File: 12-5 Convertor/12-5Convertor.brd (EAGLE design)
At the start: 29.6 x 41.3 mm, 14 parts, among them U1 LM2678

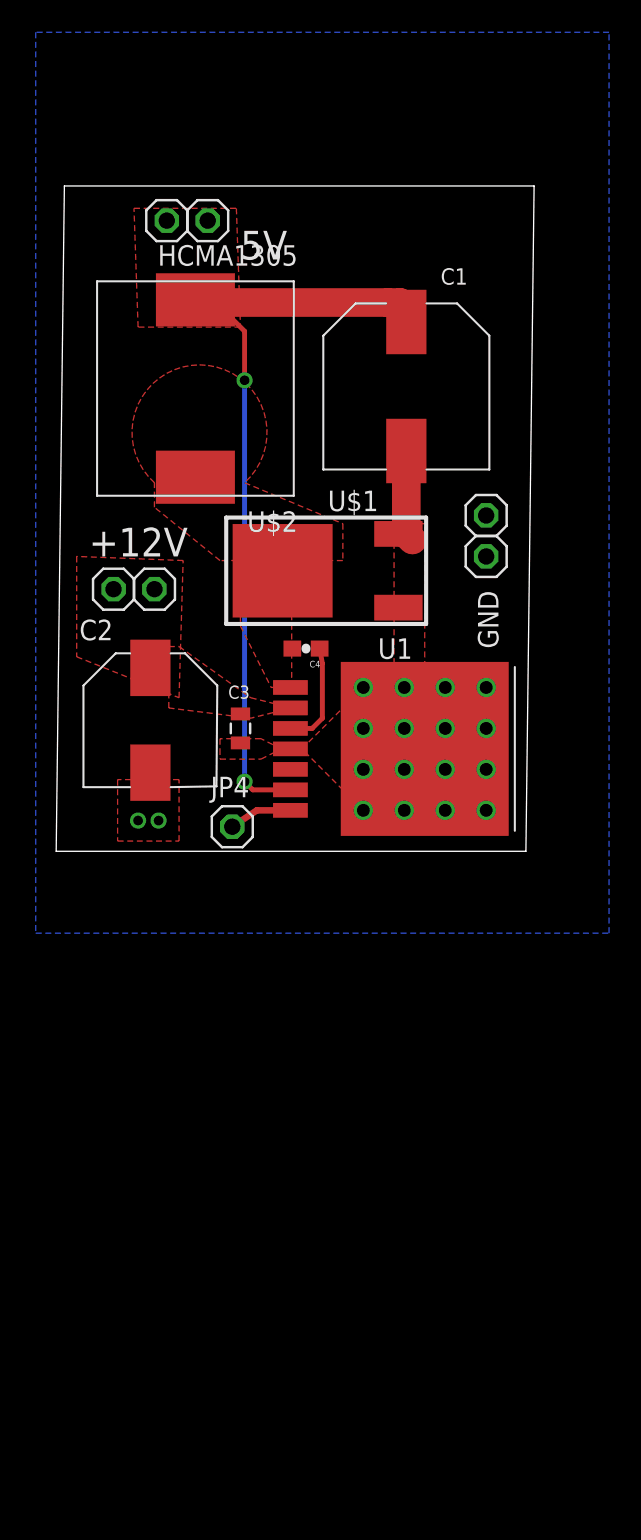
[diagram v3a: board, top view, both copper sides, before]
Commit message: Put finishing touches on buck regulator test board
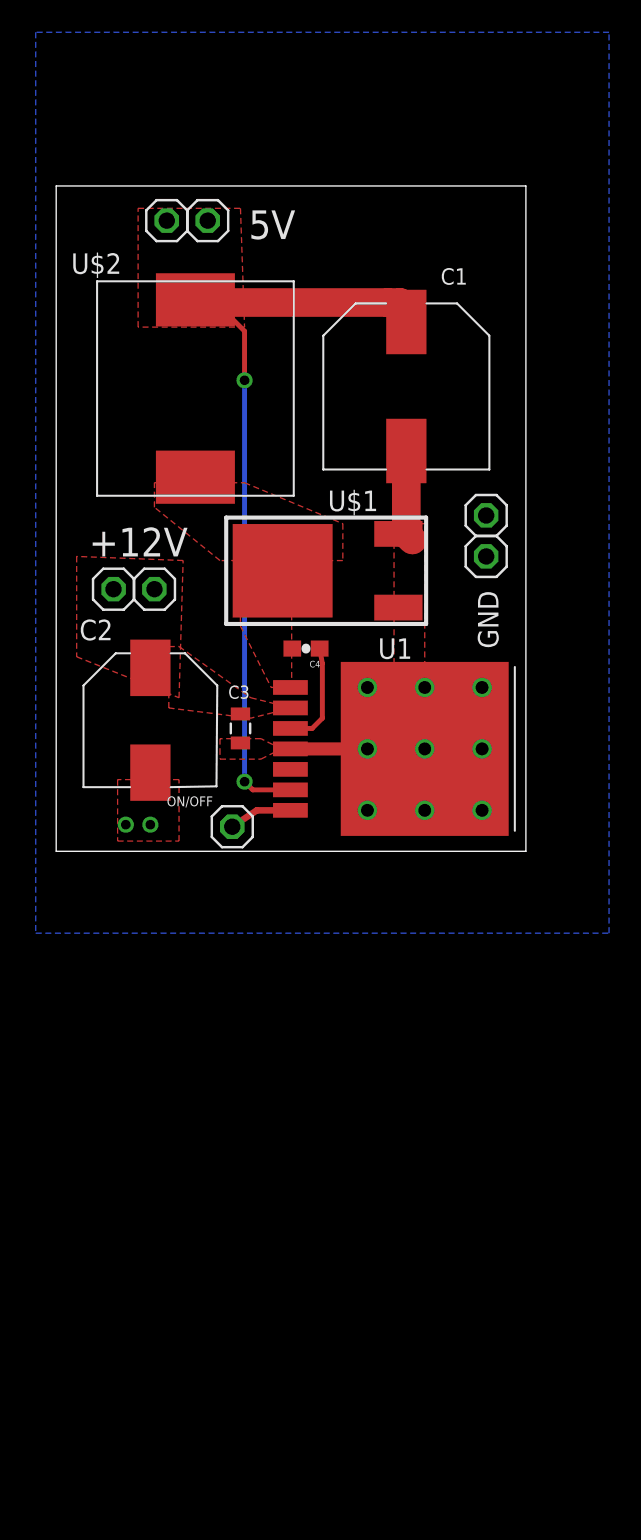
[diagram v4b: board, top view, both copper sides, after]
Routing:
- net GND: track 5.68 -> 10.5 mm, vias 18 -> 11
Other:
- board size 29.6 x 41.3 mm -> 29.1 x 41.3 mm
- board text added: "Designed by Luke McBee, Richard Shen, Jeff Geiss, and Dimcho Karakashev +12V to +5V Buck Regulator 11/8/2015"
- board text added: "ON/OFF"
- board text removed: "DC-DC 12V-5V Convertor"
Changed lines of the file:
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@@
 <plain>
 <wire x1="31.75" y1="17.78" x2="60.884" y2="17.78" width="0" layer="20"/>
-<wire x1="60.884" y1="17.78" x2="61.392" y2="59.045" width="0" layer="20"/>
-<wire x1="61.392" y1="59.045" x2="32.258" y2="59.045" width="0" layer="20"/>
-<wire x1="32.258" y1="59.045" x2="31.75" y2="17.78" width="0" layer="20"/>
+<wire x1="60.884" y1="17.78" x2="60.884" y2="59.045" width="0" layer="20"/>
+<wire x1="60.884" y1="59.045" x2="31.75" y2="59.045" width="0" layer="20"/>
+<wire x1="31.75" y1="59.045" x2="31.75" y2="17.78" width="0" layer="20"/>
 <text x="33.782" y="36.068" size="1.778" layer="21">+12V</text>
-<text x="43.18" y="54.483" size="1.778" layer="21">5V</text>
+<text x="43.688" y="55.753" size="1.778" layer="21">5V</text>
 <text x="59.182" y="30.353" size="1.27" layer="21" rot="R90">GND</text>
-<text x="36.195" y="42.672" size="1.778" layer="22">DC-DC
-12V-5V
-Convertor</text>
+<text x="38.608" y="20.574" size="0.6096" layer="21">ON/OFF</text>
+<text x="41.91" y="55.372" size="1.016" layer="22" rot="MR180">Designed by Luke McBee,
+Richard Shen, Jeff Geiss,
+and Dimcho Karakashev
++12V to +5V
+Buck Regulator
+11/8/2015</text>
 </plain>
 <attributes>
@@
 <elements>
 <element name="C1" library="PowerComponents" package="CPOL-US(10.3_10.3MM)" value="330uF" x="53.467" y="46.609" smashed="yes">
-<attribute name="NAME" x="55.595" y="52.925" size="1.016" layer="25"/>
+<attribute name="NAME" x="55.595" y="52.925" size="1.016" layer="21"/>
 </element>
 <element name="C4" library="SparkFun-Passives" package="0603-CAP" value="0.01uF" x="47.244" y="30.353" rot="R180"/>
 <element name="C3" library="SparkFun-Capacitors" package="0805" value="0.47uF" x="43.18" y="25.4" smashed="yes" rot="R270">
-<attribute name="NAME" x="42.418" y="27.2415" size="0.8128" layer="25"/>
+<attribute name="NAME" x="42.418" y="27.2415" size="0.8128" layer="21"/>
 </element>
 <element name="U$1" library="PowerComponents" package="DPAK-3" value="SWITCHMODE_SCHOTTKY" x="48.895" y="35.179"/>
@@
 <attribute name="VALUE" x="36.576" y="30.861" size="1.27" layer="27"/>
 </element>
-<element name="JP4" library="pinhead" package="1X01" value="" x="42.672" y="19.304"/>
+<element name="JP4" library="pinhead" package="1X01" value="" x="42.672" y="19.304" smashed="yes">
+<attribute name="VALUE" x="41.402" y="16.129" size="1.27" layer="27"/>
+</element>
 <element name="JP5" library="pinhead" package="1X01" value="" x="58.42" y="38.608" smashed="yes">
 <attribute name="VALUE" x="57.15" y="35.433" size="1.27" layer="27"/>
@@
 <attribute name="VALUE" x="37.338" y="53.721" size="1.27" layer="27"/>
 </element>
-<element name="U$2" library="DiscreteComponents" package="HCMA1305" value="HCMA1305" x="40.386" y="46.482" rot="R180"/>
+<element name="U$2" library="DiscreteComponents" package="HCMA1305" value="HCMA1305" x="40.386" y="46.482" smashed="yes" rot="R180">
+<attribute name="NAME" x="35.814" y="54.864" size="1.27" layer="21" rot="R180"/>
+</element>
 <element name="C2" library="PowerComponents" package="CPOL-US(8.3_8.3MM)" value="C-ALUMINUM(47UF)" x="37.592" y="25.908" smashed="yes">
 <attribute name="NAME" x="33.186" y="30.87" size="1.27" layer="21"/>
@@
 </polygon>
 <polygon width="0.254" layer="1" thermals="no">
-<vertex x="37.846" y="40.64" curve="-276.320731"/>
+<vertex x="37.846" y="40.64"/>
 <vertex x="43.434" y="40.64"/>
 <vertex x="49.53" y="38.1"/>
@@
 <contactref element="U$1" pad="P$3"/>
 <contactref element="U$1" pad="P$1"/>
-<via x="50.8" y="25.4" extent="1-16" drill="0.8"/>
-<via x="50.8" y="22.86" extent="1-16" drill="0.8"/>
-<via x="50.8" y="20.32" extent="1-16" drill="0.8"/>
-<via x="50.8" y="27.94" extent="1-16" drill="0.8"/>
-<via x="53.34" y="27.94" extent="1-16" drill="0.8"/>
-<via x="53.34" y="25.4" extent="1-16" drill="0.8"/>
-<via x="53.34" y="22.86" extent="1-16" drill="0.8"/>
-<via x="53.34" y="20.32" extent="1-16" drill="0.8"/>
-<via x="55.88" y="20.32" extent="1-16" drill="0.8"/>
-<via x="58.42" y="20.32" extent="1-16" drill="0.8"/>
-<via x="55.88" y="22.86" extent="1-16" drill="0.8"/>
-<via x="58.42" y="22.86" extent="1-16" drill="0.8"/>
-<via x="58.42" y="25.4" extent="1-16" drill="0.8"/>
-<via x="58.42" y="27.94" extent="1-16" drill="0.8"/>
-<via x="55.88" y="27.94" extent="1-16" drill="0.8"/>
-<via x="55.88" y="25.4" extent="1-16" drill="0.8"/>
-<via x="36.83" y="19.685" extent="1-16" drill="0.6"/>
+<via x="54.61" y="24.13" extent="1-16" drill="0.8"/>
+<via x="51.054" y="24.13" extent="1-16" drill="0.8"/>
+<via x="51.054" y="20.32" extent="1-16" drill="0.8"/>
+<via x="51.054" y="27.94" extent="1-16" drill="0.8"/>
+<via x="54.61" y="20.32" extent="1-16" drill="0.8"/>
+<via x="58.166" y="20.32" extent="1-16" drill="0.8"/>
+<via x="58.166" y="24.13" extent="1-16" drill="0.8"/>
+<via x="58.166" y="27.94" extent="1-16" drill="0.8"/>
+<via x="54.61" y="27.94" extent="1-16" drill="0.8"/>
+<via x="36.068" y="19.431" extent="1-16" drill="0.6"/>
 <polygon width="0.3048" layer="16">
 <vertex x="30.48" y="12.7"/>
@@
 <vertex x="54.61" y="29.21"/>
 <vertex x="54.61" y="38.1"/>
-</polygon>
-<polygon width="0.3048" layer="1" thermals="no">
-<vertex x="50.8" y="20.32"/>
-<vertex x="46.99" y="24.13"/>
-<vertex x="50.165" y="27.305"/>
 </polygon>
 <polygon width="0.3048" layer="1" thermals="no">
@@
 <vertex x="39.37" y="22.225"/>
 </polygon>
-<via x="38.1" y="19.685" extent="1-16" drill="0.6"/>
+<via x="37.592" y="19.431" extent="1-16" drill="0.6"/>
 <wire x1="53.467" y1="42.609" x2="53.467" y2="37.465" width="1.778" layer="1"/>
 <wire x1="53.467" y1="37.465" x2="53.848" y2="37.084" width="1.778" layer="1"/>
@@
 <contactref element="U1" pad="TAB"/>
 <contactref element="C2" pad="-"/>
+<wire x1="46.2788" y1="24.13" x2="51.054" y2="24.13" width="0.8128" layer="1"/>
 </signal>
 <signal name="ON/OFF">
@@
 <wire x1="40.9829" y1="51.562" x2="40.64" y2="51.562" width="0.4064" layer="1"/>
 <polygon width="0.3048" layer="1" thermals="no">
-<vertex x="36.576" y="57.658"/>
-<vertex x="42.926" y="57.658"/>
-<vertex x="43.18" y="50.292"/>
+<vertex x="36.83" y="57.658"/>
+<vertex x="43.18" y="57.658"/>
+<vertex x="43.434" y="50.292"/>
 <vertex x="36.83" y="50.292"/>
 </polygon>
